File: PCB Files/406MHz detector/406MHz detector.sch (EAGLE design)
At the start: 18 parts, among them J1 switch

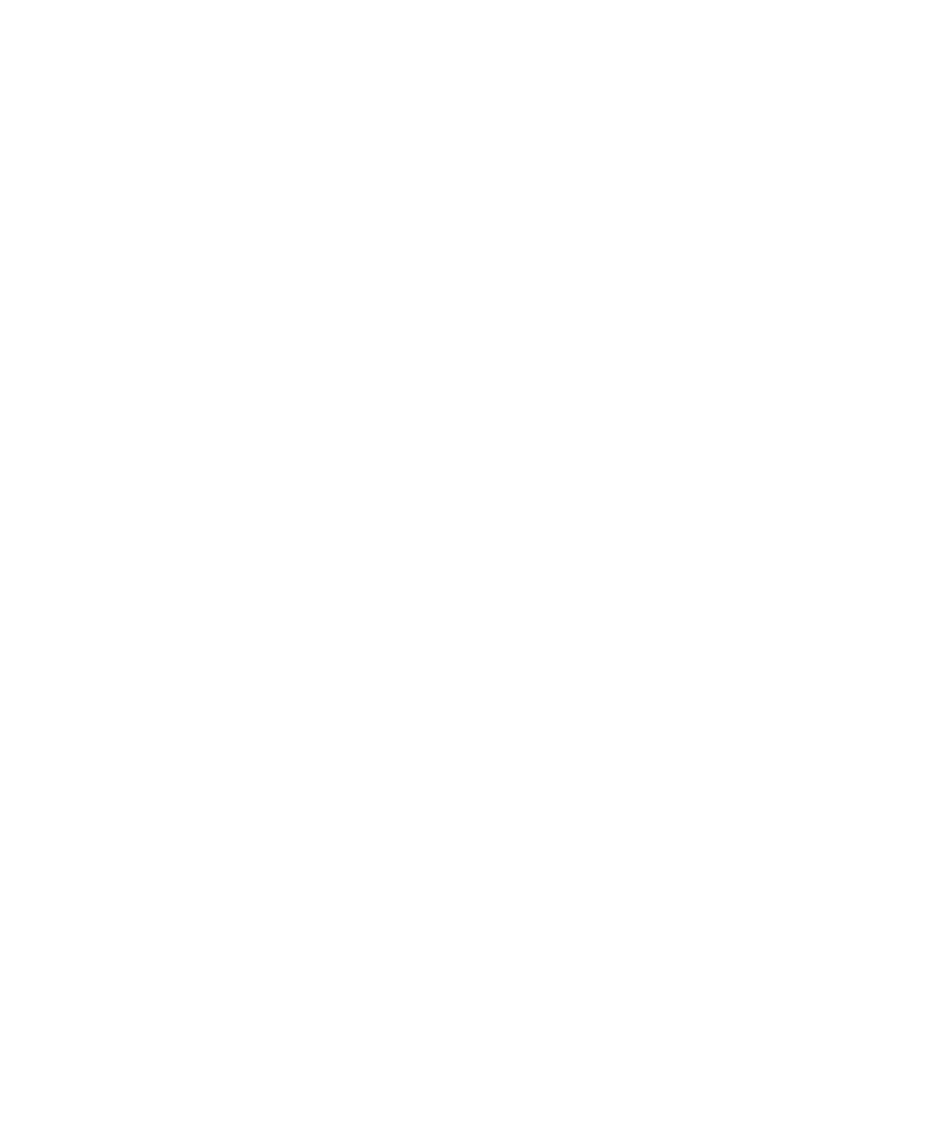
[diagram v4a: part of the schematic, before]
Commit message: added diode datasheet, added input filtering for aircraft power
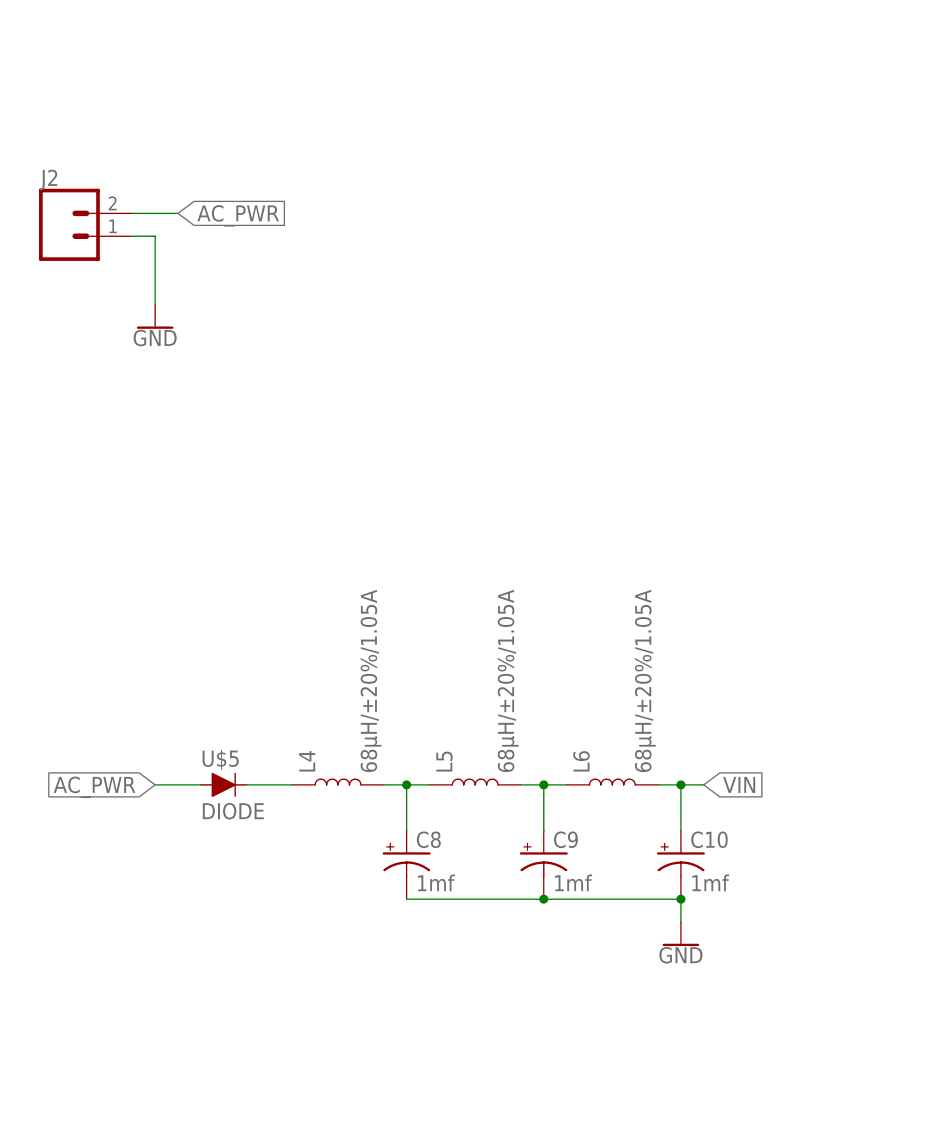
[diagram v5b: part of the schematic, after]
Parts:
- added C10, C8, C9: 1mf, SparkFun-Capacitors:1000UF-RADIAL-5MM-35V-20%-KIT
- added J2: (no value), SparkFun-Connectors:CONN_02LOCK
- added L4, L5, L6: 68µH/±20%/1.05A, SparkFun-Coils:INDUCTOR-CR75-68UH
- added U$5: DIODE, capstone:DIODE
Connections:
- new net AC_PWR: J2.2, U$5.A
- new net N$15: L4.1, U$5.C
- new net N$16: C8.+, L4.2, L5.1
- new net N$17: C9.+, L5.2, L6.1
- net GND: now also C10.-, C8.-, C9.-, J2.1
- net VIN: now also C10.+, L6.2
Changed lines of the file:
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@@
 <part name="GND7" library="SparkFun-PowerSymbols" library_urn="urn:adsk.eagle:library:530" deviceset="GND" device=""/>
 <part name="C7" library="SparkFun-Capacitors" library_urn="urn:adsk.eagle:library:510" deviceset="2.2UF" device="-0805-25V-(+80/-20%)" package3d_urn="urn:adsk.eagle:package:37429/1" value="2.2uF"/>
+<part name="L4" library="SparkFun-Coils" library_urn="urn:adsk.eagle:library:512" deviceset="INDUCTOR" device="-CR75-68UH" package3d_urn="urn:adsk.eagle:package:37573/1" value="68µH/±20%/1.05A"/>
+<part name="L5" library="SparkFun-Coils" library_urn="urn:adsk.eagle:library:512" deviceset="INDUCTOR" device="-CR75-68UH" package3d_urn="urn:adsk.eagle:package:37573/1" value="68µH/±20%/1.05A"/>
+<part name="L6" library="SparkFun-Coils" library_urn="urn:adsk.eagle:library:512" deviceset="INDUCTOR" device="-CR75-68UH" package3d_urn="urn:adsk.eagle:package:37573/1" value="68µH/±20%/1.05A"/>
+<part name="C8" library="SparkFun-Capacitors" library_urn="urn:adsk.eagle:library:510" deviceset="1000UF" device="-RADIAL-5MM-35V-20%-KIT" package3d_urn="urn:adsk.eagle:package:37421/1" value="1mf"/>
+<part name="C9" library="SparkFun-Capacitors" library_urn="urn:adsk.eagle:library:510" deviceset="1000UF" device="-RADIAL-5MM-35V-20%-KIT" package3d_urn="urn:adsk.eagle:package:37421/1" value="1mf"/>
+<part name="C10" library="SparkFun-Capacitors" library_urn="urn:adsk.eagle:library:510" deviceset="1000UF" device="-RADIAL-5MM-35V-20%-KIT" package3d_urn="urn:adsk.eagle:package:37421/1" value="1mf"/>
+<part name="U$5" library="capstone" deviceset="DIODE" device=""/>
+<part name="GND11" library="SparkFun-PowerSymbols" library_urn="urn:adsk.eagle:library:530" deviceset="GND" device=""/>
+<part name="J2" library="SparkFun-Connectors" library_urn="urn:adsk.eagle:library:513" deviceset="CONN_02" device="LOCK" package3d_urn="urn:adsk.eagle:package:38045/1"/>
+<part name="GND12" library="SparkFun-PowerSymbols" library_urn="urn:adsk.eagle:library:530" deviceset="GND" device=""/>
 </parts>
 <sheets>
@@
 <attribute name="VALUE" x="57.404" y="145.161" size="1.778" layer="96" font="vector"/>
 </instance>
+<instance part="L4" gate="G$1" x="50.8" y="236.22" smashed="yes" rot="R90">
+<attribute name="NAME" x="48.26" y="237.49" size="1.778" layer="95" font="vector" rot="R90"/>
+<attribute name="VALUE" x="53.34" y="237.49" size="1.778" layer="96" font="vector" rot="R90" align="top-left"/>
+</instance>
+<instance part="L5" gate="G$1" x="66.04" y="236.22" smashed="yes" rot="R90">
+<attribute name="NAME" x="63.5" y="237.49" size="1.778" layer="95" font="vector" rot="R90"/>
+<attribute name="VALUE" x="68.58" y="237.49" size="1.778" layer="96" font="vector" rot="R90" align="top-left"/>
+</instance>
+<instance part="L6" gate="G$1" x="81.28" y="236.22" smashed="yes" rot="R90">
+<attribute name="NAME" x="78.74" y="237.49" size="1.778" layer="95" font="vector" rot="R90"/>
+<attribute name="VALUE" x="83.82" y="237.49" size="1.778" layer="96" font="vector" rot="R90" align="top-left"/>
+</instance>
+<instance part="C8" gate="G$1" x="58.42" y="228.6" smashed="yes">
+<attribute name="NAME" x="59.436" y="229.235" size="1.778" layer="95" font="vector"/>
+<attribute name="VALUE" x="59.436" y="224.409" size="1.778" layer="96" font="vector"/>
+</instance>
+<instance part="C9" gate="G$1" x="73.66" y="228.6" smashed="yes">
+<attribute name="NAME" x="74.676" y="229.235" size="1.778" layer="95" font="vector"/>
+<attribute name="VALUE" x="74.676" y="224.409" size="1.778" layer="96" font="vector"/>
+</instance>
+<instance part="C10" gate="G$1" x="88.9" y="228.6" smashed="yes">
+<attribute name="NAME" x="89.916" y="229.235" size="1.778" layer="95" font="vector"/>
+<attribute name="VALUE" x="89.916" y="224.409" size="1.778" layer="96" font="vector"/>
+</instance>
+<instance part="U$5" gate="G$1" x="38.1" y="236.22" smashed="yes">
+<attribute name="NAME" x="35.56" y="238.252" size="1.778" layer="95" font="vector"/>
+<attribute name="VALUE" x="35.56" y="234.188" size="1.778" layer="96" font="vector" align="top-left"/>
+</instance>
+<instance part="GND11" gate="1" x="88.9" y="218.44" smashed="yes">
+<attribute name="VALUE" x="88.9" y="218.186" size="1.778" layer="96" align="top-center"/>
+</instance>
+<instance part="J2" gate="G$1" x="20.32" y="297.18" smashed="yes">
+<attribute name="VALUE" x="17.78" y="292.354" size="1.778" layer="96" font="vector"/>
+<attribute name="NAME" x="17.78" y="302.768" size="1.778" layer="95" font="vector"/>
+</instance>
+<instance part="GND12" gate="1" x="30.48" y="287.02" smashed="yes">
+<attribute name="VALUE" x="30.48" y="286.766" size="1.778" layer="96" align="top-center"/>
+</instance>
 </instances>
 <busses>
@@
 <junction x="45.72" y="185.42"/>
 <label x="40.64" y="185.42" size="1.27" layer="95" rot="R180" xref="yes"/>
+</segment>
+<segment>
+<pinref part="L6" gate="G$1" pin="2"/>
+<wire x1="86.36" y1="236.22" x2="88.9" y2="236.22" width="0.1524" layer="91"/>
+<pinref part="C10" gate="G$1" pin="+"/>
+<wire x1="88.9" y1="236.22" x2="91.44" y2="236.22" width="0.1524" layer="91"/>
+<wire x1="88.9" y1="231.14" x2="88.9" y2="236.22" width="0.1524" layer="91"/>
+<junction x="88.9" y="236.22"/>
+<label x="91.44" y="236.22" size="1.778" layer="95" xref="yes"/>
 </segment>
 </net>
@@
 <pinref part="GND7" gate="1" pin="GND"/>
 </segment>
+<segment>
+<pinref part="C8" gate="G$1" pin="-"/>
+<pinref part="C10" gate="G$1" pin="-"/>
+<wire x1="58.42" y1="223.52" x2="73.66" y2="223.52" width="0.1524" layer="91"/>
+<pinref part="C9" gate="G$1" pin="-"/>
+<wire x1="73.66" y1="223.52" x2="88.9" y2="223.52" width="0.1524" layer="91"/>
+<junction x="73.66" y="223.52"/>
+<wire x1="88.9" y1="223.52" x2="88.9" y2="220.98" width="0.1524" layer="91"/>
+<junction x="88.9" y="223.52"/>
+<pinref part="GND11" gate="1" pin="GND"/>
+</segment>
+<segment>
+<pinref part="J2" gate="G$1" pin="1"/>
+<wire x1="27.94" y1="297.18" x2="30.48" y2="297.18" width="0.1524" layer="91"/>
+<wire x1="30.48" y1="297.18" x2="30.48" y2="289.56" width="0.1524" layer="91"/>
+<pinref part="GND12" gate="1" pin="GND"/>
+</segment>
 </net>
 <net name="N$1" class="0">
@@
 </segment>
 </net>
+<net name="AC_PWR" class="0">
+<segment>
+<wire x1="30.48" y1="236.22" x2="35.56" y2="236.22" width="0.1524" layer="91"/>
+<label x="30.48" y="236.22" size="1.778" layer="95" rot="R180" xref="yes"/>
+<pinref part="U$5" gate="G$1" pin="A"/>
+</segment>
+<segment>
+<pinref part="J2" gate="G$1" pin="2"/>
+<wire x1="27.94" y1="299.72" x2="33.02" y2="299.72" width="0.1524" layer="91"/>
+<label x="33.02" y="299.72" size="1.778" layer="95" xref="yes"/>
+</segment>
+</net>
+<net name="N$15" class="0">
+<segment>
+<wire x1="40.64" y1="236.22" x2="45.72" y2="236.22" width="0.1524" layer="91"/>
+<pinref part="L4" gate="G$1" pin="1"/>
+<pinref part="U$5" gate="G$1" pin="C"/>
+</segment>
+</net>
+<net name="N$16" class="0">
+<segment>
+<pinref part="L4" gate="G$1" pin="2"/>
+<pinref part="L5" gate="G$1" pin="1"/>
+<wire x1="55.88" y1="236.22" x2="58.42" y2="236.22" width="0.1524" layer="91"/>
+<pinref part="C8" gate="G$1" pin="+"/>
+<wire x1="58.42" y1="236.22" x2="60.96" y2="236.22" width="0.1524" layer="91"/>
+<wire x1="58.42" y1="231.14" x2="58.42" y2="236.22" width="0.1524" layer="91"/>
+<junction x="58.42" y="236.22"/>
+</segment>
+</net>
+<net name="N$17" class="0">
+<segment>
+<pinref part="L5" gate="G$1" pin="2"/>
+<pinref part="L6" gate="G$1" pin="1"/>
+<wire x1="71.12" y1="236.22" x2="73.66" y2="236.22" width="0.1524" layer="91"/>
+<pinref part="C9" gate="G$1" pin="+"/>
+<wire x1="73.66" y1="236.22" x2="76.2" y2="236.22" width="0.1524" layer="91"/>
+<wire x1="73.66" y1="231.14" x2="73.66" y2="236.22" width="0.1524" layer="91"/>
+<junction x="73.66" y="236.22"/>
+</segment>
+</net>
